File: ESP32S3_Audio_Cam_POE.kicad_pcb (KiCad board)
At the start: 4 copper layers, 56 parts, among them J1 USB-C, U1 USBLC6-2SC6, U2 TLV62568DBVR, U3 ESP32-S3R8, Y1 40MHz, Y2 32.768KHz

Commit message: Draft commit, needs routing, schematic is probably mostly OK. Footprints are roughly located.
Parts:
- removed G***: LOGO, LOGO
- removed LED1: WS2812C-2020-V1, PCM_JLCPCB:LED-SMD_4P-L1.6-W1.5_XL-1615RGBC-WS2812B
- removed TP10: TestPoint, TestPoint:TestPoint_Pad_D1.0mm
- added BOOT2: SW_BOOT, Button_Switch_SMD:SW_SPST_EVQP2, F.Cu at (53.4, 117.4)
- added C1: 4.7uF, PCM_JLCPCB:C_0805, F.Cu at (128.4, 114.4)
- added C2: 1nF, PCM_JLCPCB:C_0402, F.Cu at (126.6, 115.2)
- added C27: 100nF, PCM_JLCPCB:C_0603, F.Cu at (74.1, 93.5)
- added C28: 100nF, PCM_JLCPCB:C_0603, B.Cu at (71.7, 131.5)
- added C29: 100nF, PCM_JLCPCB:C_0603, B.Cu at (71.9, 136.8)
- added C3: 10pF, PCM_JLCPCB:C_0402, F.Cu at (76.9, 78.3)
- added C30: 100nF, PCM_JLCPCB:C_0603, F.Cu at (74.1, 95.8)
- added C31: 100nF, PCM_JLCPCB:C_0603, B.Cu at (69.7, 131.5)
- added C32: 100nF, PCM_JLCPCB:C_0603, B.Cu at (69.7, 132.8)
- added C33: 10pF, PCM_JLCPCB:C_0402, F.Cu at (101.8, 119.0)
- added C34: 10pF, PCM_JLCPCB:C_0402, F.Cu at (105.0, 122.3)
- added C35: 100nF, PCM_JLCPCB:C_0603, B.Cu at (114.2, 125.3)
- added C36: 10uF, PCM_JLCPCB:C_0805, B.Cu at (117.9, 124.3)
- added C37: 100nF, PCM_JLCPCB:C_0603, B.Cu at (112.8, 125.3)
- added C38: 100nF, PCM_JLCPCB:C_0603, F.Cu at (66.9, 94.8)
- added C39: 10nF, PCM_JLCPCB:C_0402, F.Cu at (101.8, 124.3)
- added C4: 10pF, PCM_JLCPCB:C_0402, F.Cu at (70.8, 123.7)
- added C40: 4.7uF, PCM_JLCPCB:C_0603, B.Cu at (115.5, 125.3)
- added C41: 100nF, PCM_JLCPCB:C_0603, F.Cu at (90.2, 142.3)
- added C42: 1uF, PCM_JLCPCB:C_0603, F.Cu at (87.9, 142.3)
- added C43: 1uF, PCM_JLCPCB:C_0603, B.Cu at (90.7, 40.8)
- added C44: 100nF, PCM_JLCPCB:C_0603, B.Cu at (90.7, 43.3)
- added C45: 100pF, PCM_JLCPCB:C_0402, B.Cu at (100.7, 35.8)
- added C46: 100nF, PCM_JLCPCB:C_0603, F.Cu at (99.1, 87.7)
- added C47: 100pF, PCM_JLCPCB:C_0402, B.Cu at (93.4, 39.8)
- added C48: 1uF, PCM_JLCPCB:C_0603, F.Cu at (99.1, 89.2)
- added C49: 100nF, PCM_JLCPCB:C_0603, F.Cu at (91.2, 153.8)
- added C5: 100nF, PCM_JLCPCB:C_0603, F.Cu at (124.6, 115.2)
- added C50: 6.8nF, PCM_JLCPCB:C_0603, F.Cu at (128.8, 122.8)
- added C51: 6.8nF, PCM_JLCPCB:C_0603, F.Cu at (128.8, 125.8)
- added C52: 220nF, PCM_JLCPCB:C_0603, F.Cu at (128.8, 131.8)
- added C53: 220nF, PCM_JLCPCB:C_0603, F.Cu at (128.8, 124.3)
- added C54: 10uF, PCM_JLCPCB:C_0805, F.Cu at (118.9, 98.3)
- added C55: 100nF, PCM_JLCPCB:C_0603, F.Cu at (120.7, 98.3)
- added C56: 100nF, PCM_JLCPCB:C_0603, F.Cu at (62.5, 81.0)
- added C57: 100nF, PCM_JLCPCB:C_0603, F.Cu at (57.9, 124.9)
- added C58: 100nF, PCM_JLCPCB:C_0603, F.Cu at (96.6, 152.0)
- added C59: 100nF, PCM_JLCPCB:C_0805, B.Cu at (143.3, 137.3)
- added C60: 100nF, PCM_JLCPCB:C_0805, F.Cu at (146.3, 137.3)
- added C61: 10uF, PCM_JLCPCB:C_0805, B.Cu at (140.3, 144.8)
- added C62: 100nF, PCM_JLCPCB:C_0805, B.Cu at (146.8, 114.8)
- added C63: 100nF, PCM_JLCPCB:C_0805, B.Cu at (143.3, 115.3)
- added C64: 22uF, PCM_JLCPCB:C_0805, B.Cu at (140.3, 142.8)
- added C65: 1nF, PCM_JLCPCB:C_1206, B.Cu at (139.3, 135.5)
- added C66: 220pF, PCM_JLCPCB:C_0402, B.Cu at (122.9, 99.0)
- added C67: 220pF, PCM_JLCPCB:C_0402, B.Cu at (122.9, 97.0)
- added C68: 100nF, PCM_JLCPCB:C_0603, F.Cu at (62.2, 75.8)
- added C69: 100nF, PCM_JLCPCB:C_0603, F.Cu at (57.9, 117.3)
- added C70: 100nF, PCM_JLCPCB:C_0603, F.Cu at (132.0, 131.8)
- added C71: 100nF, PCM_JLCPCB:C_0603, F.Cu at (133.4, 90.0)
- added C72: 100nF, PCM_JLCPCB:C_0603, F.Cu at (48.4, 83.4)
- added CARD1: TF PUSH, JLCPCB:TF-PUSH-SD-CARD_C393941, F.Cu at (54.9, 97.8)
- added D10: Red, PCM_JLCPCB:D_0603, F.Cu at (134.9, 114.2)
- added D11: 1N4148W, PCM_JLCPCB:D_SOD-123, B.Cu at (143.6, 144.3)
- added D12: White, PCM_JLCPCB:D_0603, F.Cu at (81.3, 151.8)
- added D13: IR, JLCPCB:IR-LED_C131280, F.Cu at (84.5, 158.5)
- added D3: Yellow, PCM_JLCPCB:D_0805, F.Cu at (102.1, 114.8)
- added D4: Green, PCM_JLCPCB:D_0805, F.Cu at (102.1, 117.5)
- added D5: MB6S, JLCPCB:MB6S-C82584, B.Cu at (131.6, 151.3)
- added D6: MB6S, JLCPCB:MB6S-C82584, B.Cu at (142.1, 151.3)
- added D7: SMAJ58A, PCM_JLCPCB:D_SMA, B.Cu at (138.3, 156.0)
- added D8: Green, PCM_JLCPCB:D_0805, F.Cu at (124.9, 111.2)
- added D9: WS2812B, PCM_JLCPCB:LED-SMD_4P-L1.6-W1.5_XL-1615RGBC-WS2812B, F.Cu at (98.9, 151.0)
- added DISP1: SLS0563DRA1GD, JLCPCB:3x7-seg_LED-RED_C2913084, F.Cu at (100.7, 43.3)
- added FPC1: AFC01-S24FCC-00, JLCPCB:OV2640_connector_AFC01-S24FCC-00, F.Cu at (69.9, 64.8)
- added J10: Conn_01x02, Connector_PinHeader_1.00mm:PinHeader_1x02_P1.00mm_Vertical, B.Cu at (126.4, 98.6)
- added J11: Conn_01x02, Connector_PinHeader_1.00mm:PinHeader_1x02_P1.00mm_Vertical, F.Cu at (84.0, 162.8)
- added J12: Conn_01x02, Connector_PinHeader_1.00mm:PinHeader_1x02_P1.00mm_Vertical, F.Cu at (84.0, 156.3)
- added J13: Conn_01x02, Connector_PinHeader_1.00mm:PinHeader_1x02_P1.00mm_Vertical, F.Cu at (84.0, 153.0)
- added J2: USB-C, Connector_USB:USB_C_Receptacle_GCT_USB4105-xx-A_16P_TopMnt_Horizontal, F.Cu at (112.8, 155.5)
- added J3: Conn_01x02, Connector_PinHeader_1.00mm:PinHeader_1x02_P1.00mm_Vertical, F.Cu at (82.1, 96.4)
- added J4: Conn_01x02, Connector_PinHeader_1.00mm:PinHeader_1x02_P1.00mm_Vertical, F.Cu at (73.4, 121.0)
- added J5: Conn_01x03, Connector_PinHeader_2.54mm:PinHeader_1x03_P2.54mm_Vertical, F.Cu at (55.5, 154.5)
- added J6: Conn_01x03, Connector_PinHeader_2.54mm:PinHeader_1x03_P2.54mm_Vertical, F.Cu at (60.1, 154.5)
- added J7: Conn_01x03, Connector_PinHeader_2.54mm:PinHeader_1x03_P2.54mm_Vertical, F.Cu at (64.7, 154.5)
- added J8: Conn_01x03, Connector_PinHeader_2.54mm:PinHeader_1x03_P2.54mm_Vertical, F.Cu at (69.3, 154.5)
- added J9: HC-RJ45-055-4_8P8C_Shielded, JLCPCB:HC-RJ45-055-4_C3000211, F.Cu at (143.5, 126.3)
- added JP1: Jumper_2_Small_Bridged, Jumper:SolderJumper-2_P1.3mm_Bridged_RoundedPad1.0x1.5mm, F.Cu at (78.2, 96.7)
- added JP2: Jumper_2_Small_Bridged, Jumper:SolderJumper-2_P1.3mm_Bridged_RoundedPad1.0x1.5mm, F.Cu at (78.2, 100.2)
- added JP3: SolderJumper_2_Open, Jumper:SolderJumper-2_P1.3mm_Open_TrianglePad1.0x1.5mm, B.Cu at (117.9, 105.5)
- added JP4: SolderJumper_2_Open, Jumper:SolderJumper-2_P1.3mm_Open_TrianglePad1.0x1.5mm, B.Cu at (117.9, 103.0)
- added JP5: SolderJumper_2_Open, Jumper:SolderJumper-2_P1.3mm_Open_TrianglePad1.0x1.5mm, F.Cu at (117.9, 103.0)
- added JP6: SolderJumper_2_Open, Jumper:SolderJumper-2_P1.3mm_Open_TrianglePad1.0x1.5mm, F.Cu at (117.9, 105.5)
- added JP7: SolderJumper_3_Bridged12, Jumper:SolderJumper-3_P1.3mm_Bridged12_Pad1.0x1.5mm, F.Cu at (139.4, 90.3)
- added JP8: SolderJumper_3_Bridged12, Jumper:SolderJumper-3_P1.3mm_Bridged12_Pad1.0x1.5mm, F.Cu at (48.6, 77.9)
- added L4: 3.9nH,300mA, PCM_JLCPCB:L_0402, B.Cu at (114.4, 123.3)
- added PB1: SW_RST, Button_Switch_SMD:SW_SPST_EVQP2, F.Cu at (75.6, 36.6)
- added PB2: SW_RST, Button_Switch_SMD:SW_SPST_EVQP2, F.Cu at (127.4, 36.8)
- added Q1: AO3401A, PCM_JLCPCB:Q_SOT-23, B.Cu at (80.7, 69.1)
- added Q2: AO3401A, PCM_JLCPCB:Q_SOT-23, F.Cu at (51.1, 157.1)
- added Q3: AO3401A, PCM_JLCPCB:Q_SOT-23, F.Cu at (77.3, 153.8)
- added Q4: AO3401A, PCM_JLCPCB:Q_SOT-23, F.Cu at (77.3, 158.5)
- added Q5: AO3401A, PCM_JLCPCB:Q_SOT-23, F.Cu at (77.3, 163.8)
- added R13: 33Ω, PCM_JLCPCB:R_0402, F.Cu at (114.3, 149.0)
- added R14: 10MΩ, PCM_JLCPCB:R_0402, B.Cu at (81.9, 66.6)
- added R15: 1MΩ, PCM_JLCPCB:R_0402, B.Cu at (79.9, 66.6)
- added R16: 10kΩ, PCM_JLCPCB:R_0402, B.Cu at (70.2, 60.1)
- added R17: 10kΩ, PCM_JLCPCB:R_0402, B.Cu at (70.2, 61.1)
- added R18: 10kΩ, PCM_JLCPCB:R_0402, B.Cu at (70.2, 62.1)
- added R19: 10kΩ, PCM_JLCPCB:R_0402, B.Cu at (68.5, 62.1)
- added R20: 1MΩ, PCM_JLCPCB:R_0402, F.Cu at (99.3, 121.5)
- added R21: 0Ω, PCM_JLCPCB:R_0402, F.Cu at (105.0, 123.3)
- added R22: 20Ω, PCM_JLCPCB:R_0603, F.Cu at (105.4, 126.8)
- added R23: 20Ω, PCM_JLCPCB:R_0603, F.Cu at (105.4, 128.3)
- added R24: 20Ω, PCM_JLCPCB:R_0603, F.Cu at (105.4, 129.8)
- added R25: 20Ω, PCM_JLCPCB:R_0603, F.Cu at (105.4, 131.3)
- added R26: 20Ω, PCM_JLCPCB:R_0603, F.Cu at (105.4, 132.8)
- added R27: 20Ω, PCM_JLCPCB:R_0603, F.Cu at (105.4, 134.3)
- added R28: 10kΩ, PCM_JLCPCB:R_0402, F.Cu at (114.8, 117.8)
- added R29: 10kΩ, PCM_JLCPCB:R_0402, F.Cu at (63.1, 97.8)
- added R3: 22Ω, PCM_JLCPCB:R_0402, B.Cu at (130.1, 111.4)
- added R30: 10kΩ, PCM_JLCPCB:R_0402, F.Cu at (64.6, 97.3)
- added R31: 10kΩ, PCM_JLCPCB:R_0402, F.Cu at (64.6, 95.3)
- added R32: 10kΩ, PCM_JLCPCB:R_0402, F.Cu at (65.6, 94.8)
- added R33: 100kΩ, PCM_JLCPCB:R_0402, F.Cu at (86.2, 135.2)
- added R34: 680Ω, PCM_JLCPCB:R_0402, F.Cu at (105.1, 114.8)
- added R35: 680Ω, PCM_JLCPCB:R_0402, F.Cu at (105.1, 120.0)
- added R36: 12kΩ, PCM_JLCPCB:R_0603, F.Cu at (122.5, 124.8)
- added R37: 100kΩ, PCM_JLCPCB:R_0402, F.Cu at (99.1, 90.4)
- added R38: 10kΩ, PCM_JLCPCB:R_0402, B.Cu at (92.4, 42.0)
- added R39: 10kΩ, PCM_JLCPCB:R_0402, B.Cu at (93.4, 42.0)
- added R4: 5.1kΩ, PCM_JLCPCB:R_0402, B.Cu at (144.7, 98.5)
- added R40: 100kΩ, PCM_JLCPCB:R_0805, B.Cu at (115.2, 104.3)
- added R41: 100kΩ, PCM_JLCPCB:R_0805, F.Cu at (115.2, 104.3)
- added R42: 10MΩ, PCM_JLCPCB:R_0402, F.Cu at (48.3, 157.1)
- added R43: 1MΩ, PCM_JLCPCB:R_0402, B.Cu at (116.9, 98.0)
- added R44: 47Ω, PCM_JLCPCB:R_0603, F.Cu at (128.8, 128.8)
- added R45: 47Ω, PCM_JLCPCB:R_0603, F.Cu at (128.8, 130.3)
- added R46: 47Ω, PCM_JLCPCB:R_0603, F.Cu at (128.8, 133.3)
- added R47: 1MΩ, PCM_JLCPCB:R_0402, F.Cu at (48.3, 155.1)
- added R48: 82Ω, PCM_JLCPCB:R_0603, F.Cu at (131.3, 122.8)
- added R49: 82Ω, PCM_JLCPCB:R_0603, F.Cu at (131.3, 125.8)
- added R50: 10kΩ, PCM_JLCPCB:R_0402, F.Cu at (124.9, 112.7)
- added R51: 10kΩ, PCM_JLCPCB:R_0402, F.Cu at (62.5, 83.5)
- added R52: 10kΩ, PCM_JLCPCB:R_0402, F.Cu at (57.9, 127.4)
- added R53: 10kΩ, PCM_JLCPCB:R_0402, F.Cu at (136.1, 114.2)
- added R54: 10MΩ, PCM_JLCPCB:R_0402, F.Cu at (74.5, 153.8)
- added R55: 10MΩ, PCM_JLCPCB:R_0402, F.Cu at (74.5, 158.8)
- added R56: 10MΩ, PCM_JLCPCB:R_0402, F.Cu at (74.5, 163.8)
- added R57: 1MΩ, PCM_JLCPCB:R_0402, F.Cu at (74.5, 151.8)
- added R58: 1MΩ, PCM_JLCPCB:R_0402, F.Cu at (74.5, 156.8)
- added R59: 75Ω, PCM_JLCPCB:R_0603, F.Cu at (134.3, 129.3)
- added R60: 75Ω, PCM_JLCPCB:R_0603, F.Cu at (135.5, 129.3)
- added R61: 75Ω, PCM_JLCPCB:R_0603, F.Cu at (135.3, 133.3)
- added R62: 75Ω, PCM_JLCPCB:R_0603, F.Cu at (135.3, 131.8)
- added R63: 1MΩ, PCM_JLCPCB:R_0402, F.Cu at (74.5, 161.8)
- added R64: 10kΩ, PCM_JLCPCB:R_0402, F.Cu at (80.5, 158.5)
- added R65: 10kΩ, PCM_JLCPCB:R_0402, F.Cu at (80.5, 153.8)
- added RST2: SW_RST, Button_Switch_SMD:SW_SPST_EVQP2, F.Cu at (53.4, 124.9)
- added T1: H1102NLT, JLCPCB:H1102NLT_C18584, B.Cu at (130.6, 127.3)
- added TP11: TestPoint, TestPoint:TestPoint_Pad_D1.0mm, B.Cu at (68.5, 57.8)
- added TP12: TestPoint, TestPoint:TestPoint_Pad_D1.0mm, B.Cu at (71.2, 68.6)
- added TP13: TestPoint, TestPoint:TestPoint_Pad_D1.0mm, B.Cu at (70.5, 70.6)
- added TP14: TestPoint, TestPoint:TestPoint_Plated_Hole_D2.0mm, B.Cu at (71.2, 55.1)
- added TP15: TestPoint, TestPoint:TestPoint_Plated_Hole_D2.0mm, B.Cu at (71.2, 74.6)
- added TP16: TestPoint, TestPoint:TestPoint_Pad_D1.0mm, F.Cu at (73.7, 98.4)
- added TP17: TestPoint, TestPoint:TestPoint_Pad_D1.0mm, F.Cu at (80.4, 145.0)
- added TP18: TestPoint, TestPoint:TestPoint_Pad_D1.0mm, F.Cu at (91.4, 132.8)
- added TP19: TestPoint, TestPoint:TestPoint_Pad_D1.0mm, F.Cu at (91.4, 129.5)
- added TP20: TestPoint, TestPoint:TestPoint_Pad_D1.0mm, F.Cu at (91.4, 126.5)
- added TP21: TestPoint, TestPoint:TestPoint_Pad_D1.0mm, F.Cu at (91.4, 123.3)
- added TP22: TestPoint, TestPoint:TestPoint_Pad_D1.0mm, F.Cu at (91.4, 120.3)
- added TP23: TestPoint, TestPoint:TestPoint_Pad_D1.0mm, F.Cu at (91.4, 117.5)
- added TP24: TestPoint, TestPoint:TestPoint_Pad_D1.0mm, F.Cu at (91.4, 114.8)
- added TP25: TestPoint, TestPoint:TestPoint_Pad_D1.0mm, F.Cu at (91.4, 111.8)
- added TP26: TestPoint, TestPoint:TestPoint_Pad_D1.0mm, F.Cu at (84.7, 111.0)
- added TP27: TestPoint, TestPoint:TestPoint_Pad_D1.0mm, F.Cu at (81.4, 111.0)
- added TP28: TestPoint, TestPoint:TestPoint_Pad_D1.0mm, F.Cu at (76.9, 111.0)
- added TP29: TestPoint, TestPoint:TestPoint_Pad_D1.0mm, F.Cu at (73.9, 111.0)
- added TP30: TestPoint, TestPoint:TestPoint_Pad_D1.0mm, F.Cu at (71.2, 111.0)
- added TP31: TestPoint, TestPoint:TestPoint_Pad_D1.0mm, F.Cu at (68.2, 111.0)
- added TP32: TestPoint, TestPoint:TestPoint_Pad_D1.0mm, F.Cu at (57.2, 111.0)
- added TP33: TestPoint, TestPoint:TestPoint_Pad_D1.0mm, F.Cu at (119.9, 138.8)
- added TP34: TestPoint, TestPoint:TestPoint_Pad_D1.0mm, F.Cu at (117.9, 138.8)
- added TP35: TestPoint, TestPoint:TestPoint_Pad_D1.0mm, F.Cu at (115.9, 138.8)
- added TP36: TestPoint, TestPoint:TestPoint_Pad_D1.0mm, F.Cu at (105.9, 138.8)
- added TP37: TestPoint, TestPoint:TestPoint_Pad_D1.0mm, F.Cu at (107.9, 138.8)
- added TP38: TestPoint, TestPoint:TestPoint_Pad_D1.0mm, F.Cu at (109.9, 138.8)
- added TP39: TestPoint, TestPoint:TestPoint_Pad_D1.0mm, F.Cu at (111.9, 138.8)
- added TP40: TestPoint, TestPoint:TestPoint_Pad_D1.0mm, F.Cu at (113.9, 138.8)
- added TP41: TestPoint, TestPoint:TestPoint_Pad_D1.0mm, F.Cu at (111.4, 113.8)
- added TP42: TestPoint, TestPoint:TestPoint_Pad_D1.0mm, F.Cu at (105.8, 117.8)
- added TP43: TestPoint, TestPoint:TestPoint_Pad_D1.0mm, F.Cu at (117.7, 113.8)
- added TP44: TestPoint, TestPoint:TestPoint_Pad_D1.0mm, F.Cu at (95.9, 141.9)
- added TP45: TestPoint, TestPoint:TestPoint_Pad_D1.0mm, F.Cu at (62.9, 100.5)
- added TP46: TestPoint, TestPoint:TestPoint_Pad_D1.0mm, F.Cu at (63.4, 92.0)
- added TP47: TestPoint, TestPoint:TestPoint_Pad_D1.0mm, F.Cu at (63.4, 90.0)
- added TP48: TestPoint, TestPoint:TestPoint_Pad_D1.0mm, B.Cu at (107.9, 49.3)
- added TP49: TestPoint, TestPoint:TestPoint_Pad_D1.0mm, F.Cu at (92.8, 141.9)
- added TP50: TestPoint, TestPoint:TestPoint_Pad_D1.0mm, F.Cu at (91.2, 33.5)
- added TP51: TestPoint, TestPoint:TestPoint_Plated_Hole_D2.0mm, F.Cu at (49.6, 88.3)
- added TP52: TestPoint, TestPoint:TestPoint_Plated_Hole_D2.0mm, F.Cu at (59.1, 88.3)
- added TP53: TestPoint, TestPoint:TestPoint_Plated_Hole_D2.0mm, F.Cu at (49.6, 107.3)
- added TP54: TestPoint, TestPoint:TestPoint_Plated_Hole_D2.0mm, F.Cu at (59.4, 106.8)
- added TP55: TestPoint, TestPoint:TestPoint_Pad_D1.0mm, B.Cu at (137.0, 126.5)
- added TP56: TestPoint, TestPoint:TestPoint_Pad_D1.0mm, B.Cu at (137.0, 128.5)
- added TP57: TestPoint, TestPoint:TestPoint_Pad_D1.0mm, B.Cu at (93.2, 46.5)
- added TP58: TestPoint, TestPoint:TestPoint_Pad_D1.0mm, B.Cu at (92.9, 49.8)
- added TP59: TestPoint, TestPoint:TestPoint_Pad_D1.0mm, F.Cu at (102.6, 97.7)
- added TP6: TestPoint, TestPoint:TestPoint_Pad_D1.0mm, F.Cu at (45.7, 133.1)
- added TP60: TestPoint, TestPoint:TestPoint_Pad_D1.0mm, F.Cu at (95.6, 97.7)
- added TP61: TestPoint, TestPoint:TestPoint_Pad_D1.0mm, B.Cu at (124.0, 126.3)
- added TP62: TestPoint, TestPoint:TestPoint_Pad_D1.0mm, B.Cu at (124.0, 128.3)
- added TP63: TestPoint, TestPoint:TestPoint_Pad_D1.0mm, F.Cu at (97.6, 149.0)
- added TP64: TestPoint, TestPoint:TestPoint_Pad_D1.0mm, B.Cu at (117.7, 96.5)
- added TP65: TestPoint, TestPoint:TestPoint_Pad_D1.0mm, B.Cu at (119.7, 95.8)
- added TP66: TestPoint, TestPoint:TestPoint_Pad_D1.0mm, F.Cu at (126.1, 142.3)
- added TP67: TestPoint, TestPoint:TestPoint_Pad_D1.0mm, B.Cu at (121.2, 101.8)
- added TP68: TestPoint, TestPoint:TestPoint_Pad_D1.0mm, B.Cu at (123.2, 101.3)
- added TST-R1: 0Ω, PCM_JLCPCB:R_0603, B.Cu at (128.1, 109.7)
- added TST-R10: 0Ω, PCM_JLCPCB:R_0603, F.Cu at (82.2, 100.1)
- added TST-R11: 0Ω, PCM_JLCPCB:R_0603, B.Cu at (66.9, 131.5)
- added TST-R12: 0Ω, PCM_JLCPCB:R_0603, B.Cu at (115.0, 121.3)
- added TST-R13: 0Ω, PCM_JLCPCB:R_0603, F.Cu at (69.1, 95.5)
- added TST-R14: 0Ω, PCM_JLCPCB:R_0603, B.Cu at (90.4, 45.8)
- added TST-R15: 0Ω, PCM_JLCPCB:R_0603, F.Cu at (92.2, 156.0)
- added TST-R16: 0Ω, PCM_JLCPCB:R_0603, F.Cu at (116.7, 98.8)
- added TST-R17: 0Ω, PCM_JLCPCB:R_0603, F.Cu at (48.0, 159.6)
- added TST-R18: 0Ω, PCM_JLCPCB:R_0603, F.Cu at (117.9, 100.8)
- added TST-R19: 0Ω, PCM_JLCPCB:R_0603, F.Cu at (98.9, 152.8)
- added TST-R2: 0Ω, PCM_JLCPCB:R_0603, B.Cu at (135.6, 116.2)
- added TST-R20: 0Ω, PCM_JLCPCB:R_0603, F.Cu at (136.4, 92.5)
- added TST-R21: 0Ω, PCM_JLCPCB:R_0603, F.Cu at (81.0, 155.5)
- added TST-R22: 0Ω, PCM_JLCPCB:R_0603, F.Cu at (81.0, 160.3)
- added TST-R23: 0Ω, PCM_JLCPCB:R_0603, F.Cu at (81.0, 165.3)
- added TST-R24: 0Ω, PCM_JLCPCB:R_0603, B.Cu at (140.3, 147.3)
- added TST-R25: 0Ω, PCM_JLCPCB:R_0603, F.Cu at (133.7, 92.5)
- added TST-R26: 0Ω, PCM_JLCPCB:R_0603, F.Cu at (50.7, 83.4)
- added TST-R27: 0Ω, PCM_JLCPCB:R_0603, F.Cu at (50.7, 80.7)
- added TST-R3: 0Ω, PCM_JLCPCB:R_0603, F.Cu at (135.2, 104.5)
- added TST-R4: 0Ω, PCM_JLCPCB:R_0603, F.Cu at (116.8, 145.5)
- added TST-R5: 0Ω, PCM_JLCPCB:R_0603, F.Cu at (83.9, 83.3)
- added TST-R6: 0Ω, PCM_JLCPCB:R_0603, B.Cu at (83.4, 69.1)
- added TST-R7: 0Ω, PCM_JLCPCB:R_0603, B.Cu at (71.7, 61.1)
- added TST-R8: 0Ω, PCM_JLCPCB:R_0603, B.Cu at (76.1, 62.9)
- added TST-R9: 0Ω, PCM_JLCPCB:R_0603, B.Cu at (76.1, 68.1)
- added U10: W25Q128, PCM_JLCPCB:SOIC-8_L5.3-W5.3-P1.27-LS8.0-BL, F.Cu at (92.7, 137.5)
- added U11: TM1637, JLCPCB:digital tube drivers_c2962580, B.Cu at (100.7, 43.3)
- added U12: DS18B20U(UMW), JLCPCB:DS18B20_C695836, F.Cu at (91.2, 151.3)
- added U13: W25Q128, PCM_JLCPCB:SOIC-8_L5.3-W5.3-P1.27-LS8.0-BL, F.Cu at (99.1, 93.9)
- added U14: DP9900M-5V, JLCPCB:DP9900M_C5380106, F.Cu at (138.8, 149.3)
- added U15: MAX98357AETE+T, JLCPCB:MAX98357AETE+T_C910544, B.Cu at (120.2, 98.9)
- added U16: ICS-43434, JLCPCB:ICS-43434_C5656610, F.Cu at (135.7, 89.8)
- added U17: ICS-43434, JLCPCB:ICS-43434_C5656610, F.Cu at (48.2, 81.2)
- added U4: USBLC6-2SC6, Package_TO_SOT_SMD:SOT-23-6, F.Cu at (112.6, 145.0)
- added U5: XC6206-1.5NR, Package_TO_SOT_SMD:SOT-23-3, B.Cu at (76.8, 65.4)
- added U6: XC6206-2.8V, Package_TO_SOT_SMD:SOT-23-3, B.Cu at (76.7, 70.7)
- added U7: ESP32-S3, PCM_JLCPCB:QFN-56-1EP_7x7mm_P0.4mm_EP4x4mm_ThermalVias, F.Cu at (80.7, 90.3)
- added U8: ESP32-S3, PCM_JLCPCB:QFN-56-1EP_7x7mm_P0.4mm_EP4x4mm_ThermalVias, F.Cu at (72.6, 134.2)
- added U9: W5500, Package_QFP:LQFP-48_7x7mm_P0.5mm, F.Cu at (115.9, 126.3)
- added X1: X322525MOB4SI, PCM_JLCPCB:OSC-SMD_4P-L3.2-W2.5-BL, F.Cu at (101.8, 121.6)
- added Y3: 32.768KHz, Crystal:Crystal_SMD_3215-2Pin_3.2x1.5mm, F.Cu at (72.2, 144.5)
- C10: value 10u -> 20pF; footprint Capacitor_SMD:C_0402_1005Metric_Pad0.74x0.62mm_HandSolder -> PCM_JLCPCB:C_0402; moved to F.Cu
- C11, C20: value 1u -> 100nF; footprint Capacitor_SMD:C_0402_1005Metric_Pad0.74x0.62mm_HandSolder -> PCM_JLCPCB:C_0603
- C12, C15: value 3p3 -> 3.3pF; footprint Capacitor_SMD:C_0603_1608Metric_Pad1.08x0.95mm_HandSolder -> PCM_JLCPCB:C_0402
- C13: value 100n -> 100nF; footprint Capacitor_SMD:C_0402_1005Metric_Pad0.74x0.62mm_HandSolder -> PCM_JLCPCB:C_0603; moved to F.Cu
- C14: value 100n -> 10uF; footprint Capacitor_SMD:C_0402_1005Metric_Pad0.74x0.62mm_HandSolder -> PCM_JLCPCB:C_0402; moved to F.Cu
- C16, C18, C26: value 100n -> 1uF; footprint Capacitor_SMD:C_0402_1005Metric_Pad0.74x0.62mm_HandSolder -> PCM_JLCPCB:C_0603; moved to B.Cu
- C17, C23: value 100n -> 1uF; footprint Capacitor_SMD:C_0402_1005Metric_Pad0.74x0.62mm_HandSolder -> PCM_JLCPCB:C_0603
- C19, C21: value 10p -> 100nF; footprint Capacitor_SMD:C_0402_1005Metric_Pad0.74x0.62mm_HandSolder -> PCM_JLCPCB:C_0603
- C22: value 20p -> 15pF; footprint Capacitor_SMD:C_0402_1005Metric_Pad0.74x0.62mm_HandSolder -> PCM_JLCPCB:C_0402
- C24: value 20p -> 100nF; footprint Capacitor_SMD:C_0402_1005Metric_Pad0.74x0.62mm_HandSolder -> PCM_JLCPCB:C_0603; moved to F.Cu
- C25: value 100n -> 100nF; footprint Capacitor_SMD:C_0402_1005Metric_Pad0.74x0.62mm_HandSolder -> PCM_JLCPCB:C_0603
- C6: value 4u7 -> 10pF; footprint Capacitor_SMD:C_0402_1005Metric_Pad0.74x0.62mm_HandSolder -> PCM_JLCPCB:C_0402; moved to F.Cu
- C7: value 10u -> 10pF; footprint Capacitor_SMD:C_0402_1005Metric_Pad0.74x0.62mm_HandSolder -> PCM_JLCPCB:C_0402; moved to F.Cu
- C8: value 100n -> 10uF; footprint Capacitor_SMD:C_0402_1005Metric_Pad0.74x0.62mm_HandSolder -> PCM_JLCPCB:C_0402
- C9: value 100n -> 20pF; footprint Capacitor_SMD:C_0402_1005Metric_Pad0.74x0.62mm_HandSolder -> PCM_JLCPCB:C_0402; moved to F.Cu
- D1, D2: value LED -> 1N4148W; footprint LED_SMD:LED_0402_1005Metric_Pad0.77x0.64mm_HandSolder -> PCM_JLCPCB:D_SOD-123; moved to F.Cu
- J1, L1, L2, TP2, TP3, TP4, TP8, Y1: moved to F.Cu
- R1, R2: value 5k1 -> 22Ω; footprint Resistor_SMD:R_0402_1005Metric_Pad0.72x0.64mm_HandSolder -> PCM_JLCPCB:R_0402; moved to F.Cu
- R10: value 10k -> 33Ω; footprint Resistor_SMD:R_0402_1005Metric_Pad0.72x0.64mm_HandSolder -> PCM_JLCPCB:R_0402
- R11, R12: value 10k -> 33Ω; footprint Resistor_SMD:R_0402_1005Metric_Pad0.72x0.64mm_HandSolder -> PCM_JLCPCB:R_0402; moved to F.Cu
- R5: value 22R -> 5.1kΩ; footprint Resistor_SMD:R_0402_1005Metric_Pad0.72x0.64mm_HandSolder -> PCM_JLCPCB:R_0402
- R6: value 450k -> 5.1kΩ; footprint Resistor_SMD:R_0402_1005Metric_Pad0.72x0.64mm_HandSolder -> PCM_JLCPCB:R_0402
- R7: value 100k -> 5.1kΩ; footprint Resistor_SMD:R_0402_1005Metric_Pad0.72x0.64mm_HandSolder -> PCM_JLCPCB:R_0402; moved to F.Cu
- R8: value 100k -> 450k
- R9: value 22R -> 100kΩ; footprint Resistor_SMD:R_0402_1005Metric_Pad0.72x0.64mm_HandSolder -> PCM_JLCPCB:R_0402
- U1: value USBLC6-2SC6 -> TLV62568DBVR; footprint Package_TO_SOT_SMD:SOT-23-6 -> Package_TO_SOT_SMD:SOT-23-5
- U2: value TLV62568DBVR -> MT9221CT-06BR5; footprint Package_TO_SOT_SMD:SOT-23-5 -> JLCPCB:Current-sensor_MT9221CT-06BR5_C879632
- U3: value ESP32-S3R8 -> USBLC6-2SC6; footprint PCM_JLCPCB:QFN-56-1EP_7x7mm_P0.4mm_EP4x4mm_ThermalVias -> Package_TO_SOT_SMD:SOT-23-6
- Y2: value 32.768KHz -> 40MHz; footprint Crystal:Crystal_SMD_3215-2Pin_3.2x1.5mm -> Crystal:Crystal_SMD_3225-4Pin_3.2x2.5mm; moved to F.Cu
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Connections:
- C10 pad 1: +3V3 -> /2OSC32_OUT
- C11 pad 1: +3V3 -> Earth
- C11 pad 2: Earth -> +3V3_RF
- C13 pad 1: +3V3 -> Earth
- C13 pad 2: Earth -> +3V3
- C16 pad 1: +3V3 -> Net-(Q1-D)
- C17 pad 1: VDD_SPI -> Net-(U5-VO)
- C18 pad 1: +3V3 -> Net-(U6-VO)
- C19 pad 1: Net-(C19-Pad1) -> Earth
- C19 pad 2: Earth -> Net-(U5-VO)
- C20 pad 1: VDD_SPI -> Earth
- C20 pad 2: Earth -> Net-(U6-VO)
- C21 pad 1: /OSC_OUT -> Earth
- C21 pad 2: Earth -> /CAM.RST
- C22 pad 1: /OSC32_IN -> Earth
- C22 pad 2: Earth -> /CAM.PCLK
- C23 pad 1: +3V3 -> Earth
- C23 pad 2: Earth -> Net-(U7-VDD3P3_RTC)
- C24 pad 1: /OSC32_OUT -> Net-(U7-VDD3P3_RTC)
- C25 pad 1: /CHIP_PU -> Net-(U7-VDD3P3_RTC)
- C26 pad 1: /CHIP_BOOT -> Earth
- C26 pad 2: Earth -> Net-(U8-VDD3P3_RTC)
- C6 pad 1: VBUS -> /OSC_OUT
- C7 pad 1: +3V3 -> /2OSC_OUT
- C8 pad 1: +3V3_RF -> Net-(C8-Pad1)
- C9 pad 1: +3V3 -> /2OSC32_IN
- D1 pad 1: Earth -> VBUS
- D1 pad 2: Net-(D1-A) -> Net-(D1-Pad2)
- D2 pad 1: Earth -> VBUS
- D2 pad 2: Net-(D2-A) -> Net-(D2-Pad2)
- J1 pad A4: VBUS -> Net-(D1-Pad2)
- J1 pad A9: VBUS -> Net-(D1-Pad2)
- J1 pad B4: VBUS -> Net-(D1-Pad2)
- J1 pad B9: VBUS -> Net-(D1-Pad2)
- L1 pad 1: Net-(U2-SW) -> Net-(U1-SW)
- L1 pad 2: +3V3 -> Net-(C8-Pad1)
- L2 pad 1: +3V3_RF -> Net-(L2-Pad1)
- R1 pad 1: /USB_CC2 -> Net-(C3-Pad1)
- R1 pad 2: Earth -> /OSC_IN
- R10 pad 1: +3V3 -> /USB_PRT_D-
- R10 pad 2: /CHIP_PU -> /USB_D-
- R11 pad 1: VBUS -> /USB_PRT_D+
- R11 pad 2: Net-(D1-A) -> /USB_D+
- R12 pad 1: +3V3 -> /2USB_PRT_D-
- R12 pad 2: Net-(D2-A) -> /2USB_D-
- R2 pad 1: /USB_CC1 -> Net-(C4-Pad1)
- R2 pad 2: Earth -> /2OSC_IN
- R5 pad 1: VBUS -> /2USB_CC2
- R5 pad 2: Net-(U2-EN) -> Earth
- R6 pad 1: +3V3 -> /USB_CC1
- R6 pad 2: Net-(U2-FB) -> Earth
- R7 pad 1: Net-(U2-FB) -> /2USB_CC1
- R8 pad 1: /FLASH_QSPI_nCS -> Net-(C8-Pad1)
- R8 pad 2: VDD_SPI -> Net-(U1-FB)
- R9 pad 1: /OSC_IN -> Net-(U1-FB)
- R9 pad 2: Net-(C19-Pad1) -> Earth
- TP1 pad 1: /USB_D- -> Net-(U1-VIN)
- TP2 pad 1: /USB_D+ -> +3V3
- TP3 pad 1: VBUS -> Net-(L2-Pad1)
- TP4 pad 1: +3V3 -> /2GPIO1
- TP5 pad 1: +3V3_RF -> /2GPIO2
- TP7 pad 1: +3V3 -> /2GPIO7
- TP8 pad 1: /FLASH_QSPI_nCS -> /2GPIO8
- TP9 pad 1: VDD_SPI -> /2GPIO14
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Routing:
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- removed copper zone on B.Cu, net +3V3
- removed copper zone on F.Cu, net +3V3
- removed copper zone on In2.Cu, net +3V3
- removed copper zone on In1.Cu, net Earth
- removed copper zone on B.Cu, net Net-(U2-SW)
- removed copper zone on B.Cu, net VBUS
- removed copper zone on In2.Cu, net VBUS
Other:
- board outline added: 109.2 x 129.5 mm
- board text removed: "ANT"
- board text removed: "BOOT"
- board text removed: "CPU"
- board text removed: "ESP32 S3"
- board text removed: "ESP32S3.M.2 D.Heetkamp 27-2-25 V2"
- board text removed: "FLASH"
- board text removed: "I/O 45/46 STRAPPING"
- board text removed: "I2C(P/U Res)"
- board text removed: "INT 3V3 ENABLE"
- board text removed: "M.2 3V3 ENABLE"
- board text removed: "M.2 USB ENABLE"
- board text removed: "M.2 VBUS ENABLE"
- board text removed: "RGB IO46"
- board text removed: "RST"
- board text removed: "SPICLK(P/D Res)"
- board text removed: "USB"
- board text removed: "VBUS 3V3"
- board text removed: "Y1: 40MHz Y2: 32.8KHz"

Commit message: draft commit
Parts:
- removed RST1: SW_RST, Button_Switch_SMD:SW_SPST_EVQP2
- added RST3: Tactile Button, 160gf, PCM_JLCPCB:SW-SMD_4P-L5.1-W5.1-P3.70-LS6.5-TL-2, F.Cu at (51.4, 120.7)
- BOOT1, BOOT2: value SW_BOOT -> Tactile Button, 160gf; footprint Button_Switch_SMD:SW_SPST_EVQP2 -> PCM_JLCPCB:SW-SMD_4P-L5.1-W5.1-P3.70-LS6.5-TL-2
- J1, J2: value USB-C -> Connector, USB-TYPE-C-16P; footprint Connector_USB:USB_C_Receptacle_GCT_USB4105-xx-A_16P_TopMnt_Horizontal -> PCM_JLCPCB:TYPE-C-SMD_HX-TYPE-C-16PIN
- L1: value 2u2 -> 2.2uH
- L2, L3: value 2n2 -> 2nH
- PB1, PB2, RST2: value SW_RST -> Tactile Button, 160gf; footprint Button_Switch_SMD:SW_SPST_EVQP2 -> PCM_JLCPCB:SW-SMD_4P-L5.1-W5.1-P3.70-LS6.5-TL-2
- U10, U13: value W25Q128 -> W25Q128JVSIQ
- moved PB2 54.5 mm to (73.0, 39.4), turned to 0 degrees
- moved PB1 53.4 mm to (128.9, 39.4), turned to 0 degrees
- moved RST2 48.9 mm to (57.1, 76.2)
- moved BOOT1 6.60 mm to (57.1, 69.2)
- moved J4 6.57 mm to (73.9, 114.5)
- moved C26 6.57 mm to (70.1, 127.5)
- moved C28 6.57 mm to (72.1, 125.0)
- moved C31 6.57 mm to (70.1, 125.0)
- moved C32 6.57 mm to (70.1, 126.2)
- moved C4 6.57 mm to (71.3, 117.1)
- moved C7 6.57 mm to (66.8, 117.1)
- moved R2 6.57 mm to (70.3, 120.4)
- moved TST-R11 6.57 mm to (67.4, 125.0)
- moved U8 6.57 mm to (73.0, 127.6)
- moved Y2 6.57 mm to (69.0, 117.1)
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- renumbered C70 to C68, C71 to C69, C72 to C70, C68 to C71, C69 to C72, R6 to R5, R5 to R6, TP11 to TP10, TP12 to TP11, TP13 to TP12, TP14 to TP13, TP15 to TP14, TP16 to TP15, TP17 to TP16, TP18 to TP17, TP19 to TP18, TP20 to TP19, TP21 to TP20, TP22 to TP21, TP23 to TP22, TP24 to TP23, TP25 to TP24, TP26 to TP25, TP27 to TP26, TP28 to TP27, TP29 to TP28, TP30 to TP29, TP31 to TP30, TP32 to TP31, TP33 to TP32, TP34 to TP33, TP35 to TP34, TP36 to TP35, TP37 to TP36, TP38 to TP37, TP39 to TP38, TP40 to TP39, TP41 to TP40, TP42 to TP41, TP43 to TP42, TP44 to TP43, TP45 to TP44, TP46 to TP45, TP47 to TP46, TP48 to TP47, TP49 to TP48, TP50 to TP49, TP51 to TP50, TP52 to TP51, TP53 to TP52, TP54 to TP53, TP55 to TP54, TP56 to TP55, TP57 to TP56, TP58 to TP57, TP59 to TP58, TP60 to TP59, TP61 to TP60, TP62 to TP61, TP63 to TP62, TP64 to TP63, TP65 to TP64, TP66 to TP65, TP67 to TP66, TP68 to TP67, TST-R27 to TST-R21, TST-R21 to TST-R22, TST-R22 to TST-R23, TST-R23 to TST-R24, TST-R24 to TST-R25, TST-R25 to TST-R26, TST-R26 to TST-R27
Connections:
- BOOT1 pad 1: Earth -> /CHIP_BOOT
- BOOT1 pad 2: /CHIP_BOOT -> unconnected-(BOOT1-B-Pad2)
- BOOT2 pad 1: Earth -> /2CHIP_BOOT
- BOOT2 pad 2: /2CHIP_BOOT -> unconnected-(BOOT2-B-Pad2)
- PB1 pad 1: /7SEG.SEG1 -> unconnected-(PB1-A-Pad1)
- PB2 pad 1: /7SEG.SEG1 -> unconnected-(PB2-A-Pad1)
- R4 pad 1: /USB_CC2 -> /USB_CC1
- R5 pad 1: /USB_CC1 -> /USB_CC2
- R6 pad 1: /2USB_CC2 -> /2USB_CC1
- R7 pad 1: /2USB_CC1 -> /2USB_CC2
- RST2 pad 1: Earth -> /CHIP_PU
- RST2 pad 2: /2CHIP_PU -> unconnected-(RST2-B-Pad2)
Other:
- outline, holes or cut-outs redrawn

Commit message: draft commit
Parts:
- R8: value 450k -> 450kΩ
- Y1, Y2: value 40MHz -> 40MHz, 15pF; footprint Crystal:Crystal_SMD_3225-4Pin_3.2x2.5mm -> JLCPCB:OSC-SMD_4P-L3.2-W2.5-BL_SIT8008BI
- moved C4 0.22 mm to (71.5, 117.1)
- moved Y2 0.13 mm to (69.2, 117.1)
- moved Y1 0.07 mm to (79.9, 78.2)
- turned U4 to -90 degrees

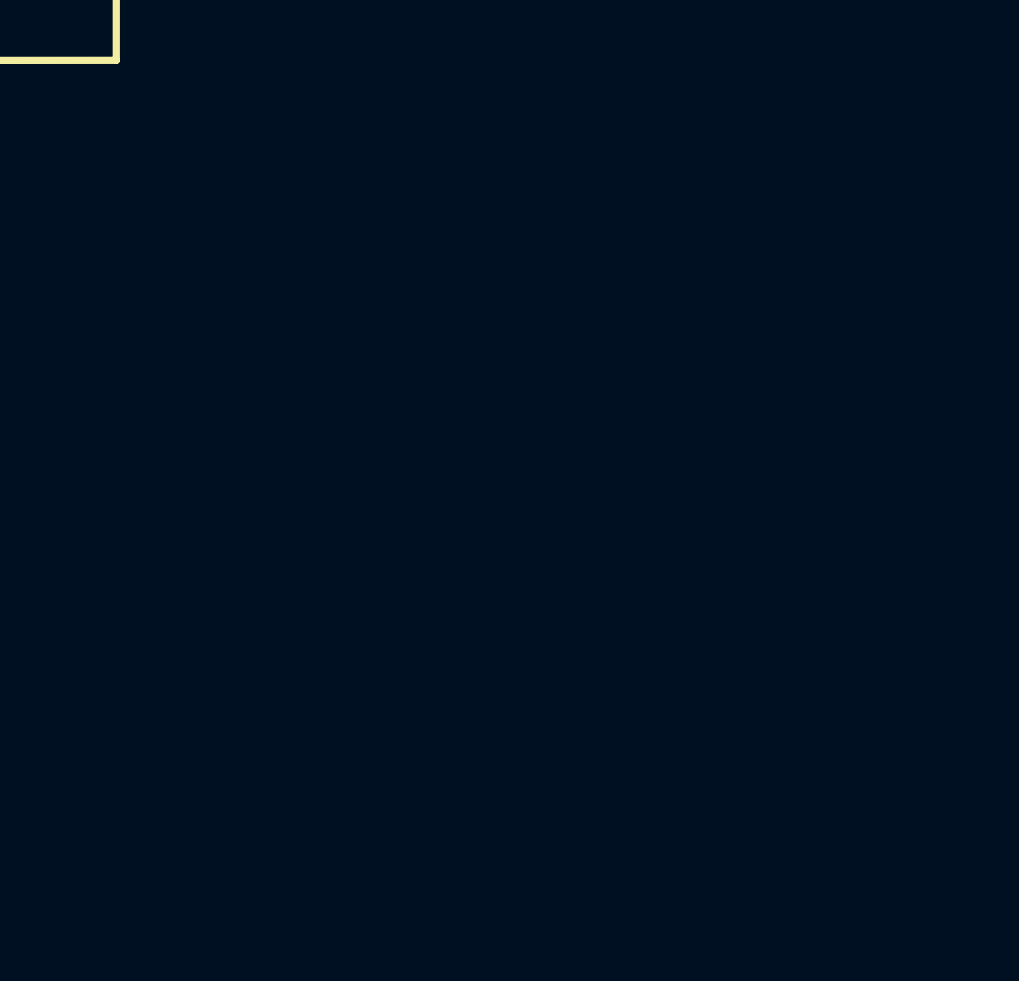
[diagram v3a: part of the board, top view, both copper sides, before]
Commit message: DRAFT added AXP2101 battery circuit
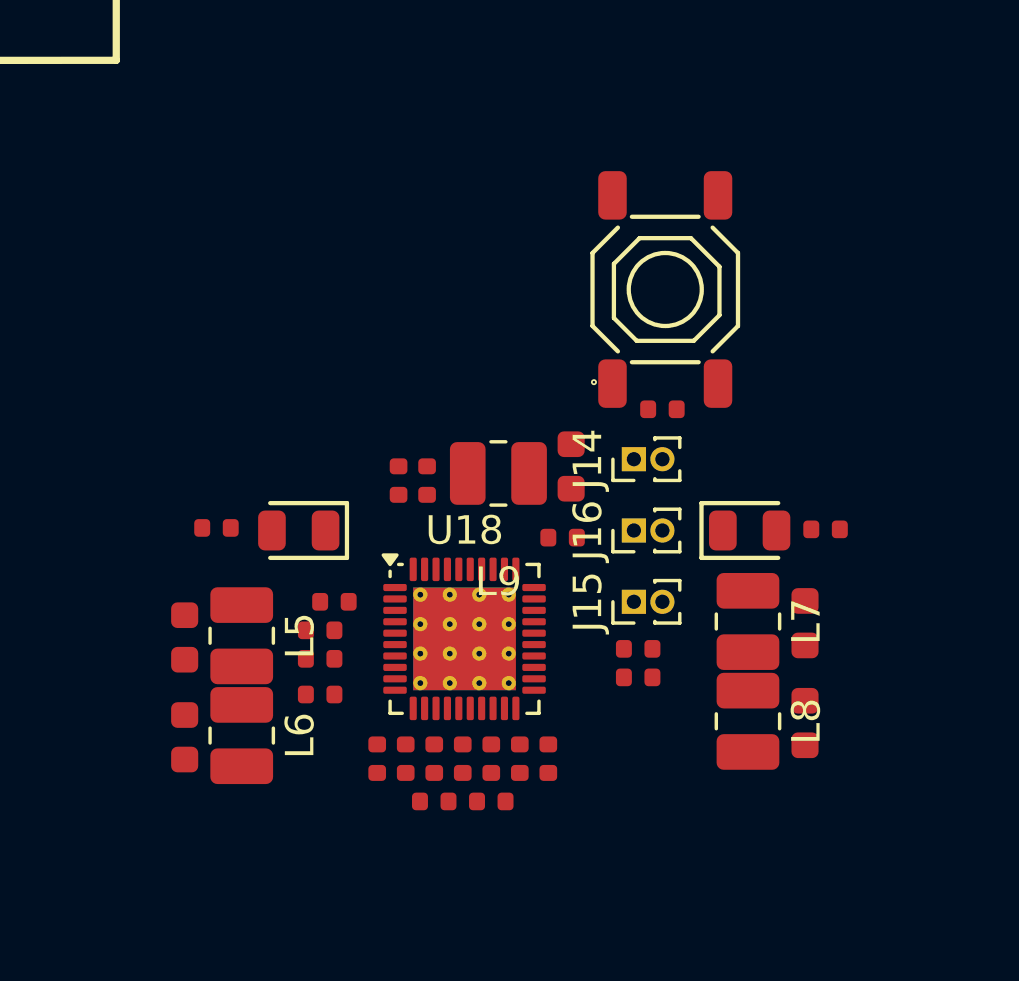
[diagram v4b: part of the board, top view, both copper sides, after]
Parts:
- added C73: 1uF, PCM_JLCPCB:C_0402, F.Cu at (127.2, 71.8)
- added C74: 10uF, PCM_JLCPCB:C_0402, F.Cu at (137.9, 74.4)
- added C75: 22uF, PCM_JLCPCB:C_0603, F.Cu at (122.0, 73.0)
- added C76: 22uF, PCM_JLCPCB:C_0603, F.Cu at (122.0, 76.5)
- added C77: 22uF, PCM_JLCPCB:C_0603, F.Cu at (143.8, 72.5)
- added C78: 22uF, PCM_JLCPCB:C_0603, F.Cu at (143.8, 76.0)
- added C79: 2.2uF, PCM_JLCPCB:C_0402, F.Cu at (132.8, 77.2)
- added C80: 2.2uF, PCM_JLCPCB:C_0402, F.Cu at (132.8, 78.8)
- added C81: 2.2uF, PCM_JLCPCB:C_0402, F.Cu at (131.8, 77.2)
- added C82: 2.2uF, PCM_JLCPCB:C_0402, F.Cu at (133.8, 77.2)
- added C83: 2.2uF, PCM_JLCPCB:C_0402, F.Cu at (134.8, 77.2)
- added C84: 2.2uF, PCM_JLCPCB:C_0402, F.Cu at (129.8, 77.2)
- added C85: 2.2uF, PCM_JLCPCB:C_0402, F.Cu at (130.8, 78.8)
- added C86: 2.2uF, PCM_JLCPCB:C_0402, F.Cu at (126.8, 75.0)
- added C87: 2.2uF, PCM_JLCPCB:C_0402, F.Cu at (128.8, 77.2)
- added C88: 1uF, PCM_JLCPCB:C_0402, F.Cu at (126.8, 73.8)
- added C89: 4.7uF, PCM_JLCPCB:C_0402, F.Cu at (129.5, 67.5)
- added C90: 1uF, PCM_JLCPCB:C_0402, F.Cu at (135.2, 69.5)
- added C91: 1uF, PCM_JLCPCB:C_0402, F.Cu at (130.5, 67.5)
- added C92: 1uF, PCM_JLCPCB:C_0402, F.Cu at (130.8, 77.2)
- added C93: 1uF, PCM_JLCPCB:C_0402, F.Cu at (126.8, 72.8)
- added C94: 1uF, PCM_JLCPCB:C_0402, F.Cu at (137.9, 73.4)
- added C95: 22uF, PCM_JLCPCB:C_0603, F.Cu at (135.6, 67.0)
- added C96: 2.2uF, PCM_JLCPCB:C_0402, F.Cu at (138.8, 65.0)
- added D14: Yellow, PCM_JLCPCB:D_0805, F.Cu at (126.0, 69.2)
- added D15: Green, PCM_JLCPCB:D_0805, F.Cu at (141.8, 69.2)
- added J14: Conn_01x02, Connector_PinHeader_1.00mm:PinHeader_1x02_P1.00mm_Vertical, F.Cu at (137.8, 66.8)
- added J15: Conn_01x02, Connector_PinHeader_1.00mm:PinHeader_1x02_P1.00mm_Vertical, F.Cu at (137.8, 71.8)
- added J16: Conn_01x02, Connector_PinHeader_1.00mm:PinHeader_1x02_P1.00mm_Vertical, F.Cu at (137.8, 69.2)
- added L5: 1uH,3.3A, Inductor_SMD:L_1008_2520Metric, F.Cu at (124.0, 72.9)
- added L6: 1uH,3.3A, Inductor_SMD:L_1008_2520Metric, F.Cu at (124.0, 76.4)
- added L7: 1uH,3.3A, Inductor_SMD:L_1008_2520Metric, F.Cu at (141.8, 72.4)
- added L8: 1uH,3.3A, Inductor_SMD:L_1008_2520Metric, F.Cu at (141.8, 75.9)
- added L9: 1uH,3.3A, Inductor_SMD:L_1008_2520Metric, F.Cu at (133.0, 67.2)
- added PB3: Tactile Button, 160gf, PCM_JLCPCB:SW-SMD_4P-L5.1-W5.1-P3.70-LS6.5-TL-2, F.Cu at (138.8, 60.8)
- added R66: 10kΩ, PCM_JLCPCB:R_0402, F.Cu at (123.1, 69.2)
- added R67: 10kΩ, PCM_JLCPCB:R_0402, F.Cu at (144.5, 69.2)
- added U18: AXP2101, Package_DFN_QFN:QFN-40-1EP_5x5mm_P0.4mm_EP3.6x3.6mm_ThermalVias, F.Cu at (131.8, 73.0)
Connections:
- net /2GPIO37 renamed /BAT.SCK
- net /2GPIO38 renamed /BAT.SDA

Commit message: DRAFT added misc outputs, PMU and resolved some TODO notes.
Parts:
- added BT1: BH-18650-B1BA002, JLCPCB:BATTERY-SMD_18650-1S-L77.1-W20.7-1, F.Cu at (169.8, 98.9)
- added C97: 22uF, PCM_JLCPCB:C_0603, F.Cu at (134.5, 64.8)
- added D16: IR, JLCPCB:IR-LED_C131280, F.Cu at (95.5, 129.0)
- added D17: IR, JLCPCB:IR-LED_C131280, F.Cu at (95.5, 122.8)
- added D18: IR, JLCPCB:IR-LED_C131280, F.Cu at (95.5, 116.6)
- added J17: Conn_01x02, Connector_PinHeader_1.00mm:PinHeader_1x02_P1.00mm_Vertical, F.Cu at (93.0, 130.5)
- added J18: Conn_01x02, Connector_PinHeader_1.00mm:PinHeader_1x02_P1.00mm_Vertical, F.Cu at (93.0, 124.2)
- added J19: Conn_01x02, Connector_PinHeader_1.00mm:PinHeader_1x02_P1.00mm_Vertical, F.Cu at (93.0, 118.1)
- added NTC1: NTC, PCM_JLCPCB:R_0402, F.Cu at (140.5, 67.0)
- added PB4: Tactile Button, 160gf, PCM_JLCPCB:SW-SMD_4P-L5.1-W5.1-P3.70-LS6.5-TL-2, F.Cu at (129.0, 48.2)
- added PB5: Tactile Button, 160gf, PCM_JLCPCB:SW-SMD_4P-L5.1-W5.1-P3.70-LS6.5-TL-2, F.Cu at (73.0, 48.2)
- added Q6: AO3401A, PCM_JLCPCB:Q_SOT-23, F.Cu at (92.3, 127.5)
- added Q7: AO3401A, PCM_JLCPCB:Q_SOT-23, F.Cu at (92.3, 121.2)
- added Q8: AO3401A, PCM_JLCPCB:Q_SOT-23, F.Cu at (92.3, 115.0)
- added R68: 100kΩ, PCM_JLCPCB:R_0402, F.Cu at (72.8, 134.0)
- added R69: 10kΩ, PCM_JLCPCB:R_0402, F.Cu at (70.8, 134.0)
- added R70: 10kΩ, PCM_JLCPCB:R_0402, F.Cu at (81.0, 128.2)
- added R71: 100kΩ, PCM_JLCPCB:R_0402, F.Cu at (81.0, 126.2)
- added R72: 100kΩ, PCM_JLCPCB:R_0402, F.Cu at (64.8, 126.8)
- added R73: 10kΩ, PCM_JLCPCB:R_0402, F.Cu at (64.8, 128.7)
- added R74: 220kΩ, PCM_JLCPCB:R_0402, F.Cu at (132.8, 110.5)
- added R75: 10kΩ, PCM_JLCPCB:R_0402, F.Cu at (132.8, 111.5)
- added R76: 220kΩ, PCM_JLCPCB:R_0402, F.Cu at (132.8, 109.5)
- added R77: 1MΩ, PCM_JLCPCB:R_0402, F.Cu at (89.8, 126.5)
- added R78: 10kΩ, PCM_JLCPCB:R_0402, F.Cu at (95.2, 126.2)
- added R79: 10MΩ, PCM_JLCPCB:R_0402, F.Cu at (89.8, 122.2)
- added R8: 10MΩ, PCM_JLCPCB:R_0402, F.Cu at (89.8, 128.5)
- added R80: 1MΩ, PCM_JLCPCB:R_0402, F.Cu at (89.8, 120.2)
- added R81: 10kΩ, PCM_JLCPCB:R_0402, F.Cu at (95.2, 120.0)
- added R82: 10MΩ, PCM_JLCPCB:R_0402, F.Cu at (89.8, 116.0)
- added R83: 1MΩ, PCM_JLCPCB:R_0402, F.Cu at (89.8, 114.0)
- added R84: 10kΩ, PCM_JLCPCB:R_0402, F.Cu at (95.2, 113.8)
- added TP68: TestPoint, TestPoint:TestPoint_Pad_D1.0mm, F.Cu at (131.0, 63.8)
- added TP69: TestPoint, TestPoint:TestPoint_Loop_D3.50mm_Drill0.9mm_Beaded, F.Cu at (187.9, 29.7)
- added TP70: TestPoint, TestPoint:TestPoint_Loop_D3.50mm_Drill0.9mm_Beaded, F.Cu at (187.9, 35.0)
- added TP71: TestPoint, TestPoint:TestPoint_Loop_D3.50mm_Drill0.9mm_Beaded, F.Cu at (187.9, 40.2)
- added TP72: TestPoint, TestPoint:TestPoint_Loop_D3.50mm_Drill0.9mm_Beaded, F.Cu at (187.9, 45.5)
- added TP73: TestPoint, TestPoint:TestPoint_Loop_D3.50mm_Drill0.9mm_Beaded, F.Cu at (193.1, 29.7)
- added TP74: TestPoint, TestPoint:TestPoint_Loop_D3.50mm_Drill0.9mm_Beaded, F.Cu at (193.1, 35.0)
- added TP75: TestPoint, TestPoint:TestPoint_Loop_D3.50mm_Drill0.9mm_Beaded, F.Cu at (193.1, 40.2)
- added TP76: TestPoint, TestPoint:TestPoint_Loop_D3.50mm_Drill0.9mm_Beaded, F.Cu at (193.1, 45.5)
- added TP77: TestPoint, TestPoint:TestPoint_Loop_D3.50mm_Drill0.9mm_Beaded, F.Cu at (198.4, 29.7)
- added TP78: TestPoint, TestPoint:TestPoint_Loop_D3.50mm_Drill0.9mm_Beaded, F.Cu at (198.4, 35.0)
- added TP79: TestPoint, TestPoint:TestPoint_Loop_D3.50mm_Drill0.9mm_Beaded, F.Cu at (198.4, 40.2)
- added TP80: TestPoint, TestPoint:TestPoint_Loop_D3.50mm_Drill0.9mm_Beaded, F.Cu at (198.4, 45.5)
- added TP81: TestPoint, TestPoint:TestPoint_Loop_D3.50mm_Drill0.9mm_Beaded, F.Cu at (203.6, 29.7)
- added TP82: TestPoint, TestPoint:TestPoint_Loop_D3.50mm_Drill0.9mm_Beaded, F.Cu at (203.6, 35.0)
- added TP83: TestPoint, TestPoint:TestPoint_Loop_D3.50mm_Drill0.9mm_Beaded, F.Cu at (203.6, 40.2)
- added TP84: TestPoint, TestPoint:TestPoint_Loop_D3.50mm_Drill0.9mm_Beaded, F.Cu at (203.6, 45.5)
- added TST-R28: 0Ω, PCM_JLCPCB:R_0603, F.Cu at (139.0, 78.2)
- added TST-R29: 0Ω, PCM_JLCPCB:R_0603, F.Cu at (137.8, 78.2)
- added TST-R30: 0Ω, PCM_JLCPCB:R_0603, F.Cu at (89.5, 130.2)
- added TST-R31: 0Ω, PCM_JLCPCB:R_0603, F.Cu at (89.5, 124.0)
- added TST-R32: 0Ω, PCM_JLCPCB:R_0603, F.Cu at (89.5, 117.8)
- moved TP17 6.89 mm to (85.0, 135.2)
- moved TP18 6.89 mm to (85.0, 132.0)
- moved TP19 6.89 mm to (85.0, 129.0)
- moved TP20 6.89 mm to (85.0, 125.8)
- moved TP21 6.89 mm to (85.0, 122.8)
- moved TP22 6.89 mm to (85.0, 120.0)
- moved TP23 6.89 mm to (85.0, 117.2)
- moved TP24 6.89 mm to (85.0, 114.2)
- moved R33 6.43 mm to (92.5, 134.0), turned to 180 degrees
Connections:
- net /2GPIO14 renamed /VBus.Sense
- net /2GPIO2 renamed /3v3.Sense
- net /2GPIO33 renamed /PMU.Vo1.Sense
- net /2GPIO34 renamed /MISC.OUT1
- net /2GPIO35 renamed /MISC.OUT2
- net /2GPIO36 renamed /MISC.OUT3
- net /BAT.SCK renamed /PMU.SCK
- net /BAT.SDA renamed /PMU.SDA
- net Net-(U18-ALDO1) renamed /PMU.Va1
- net Net-(U18-ALDO2) renamed /PMU.Va2
- net Net-(U18-ALDO3) renamed /PMU.Va3
- net Net-(U18-ALDO4) renamed /PMU.Va4
- net Net-(U18-BLDO1) renamed /PMU.Vb1
- net Net-(U18-BLDO2) renamed /PMU.Vb2
- net Net-(U18-CPULDOS) renamed /PMU.Vcpu
- net Net-(U18-DLDO1/DC1SW) renamed /PMU.Vd1
- net Net-(U18-DLDO2/DC4SW) renamed /PMU.Vd2
- net Net-(U18-FB2) renamed /PMU.Vo2
- net Net-(U18-FB3) renamed /PMU.Vo3
- net Net-(U18-LX1) renamed /PMU.Vo1
- net Net-(U18-LX4) renamed /PMU.Vo4
- C73 pad 2: Net-(U18-VREF) -> /PMU.Vref
- C74 pad 1: VBUS -> Net-(U18-VBUS)
- C88 pad 2: VBUS -> /PMU.Vsys
- C89 pad 2: VBUS -> /PMU.Vsys
- C91 pad 2: VBUS -> /PMU.Vsys
- C92 pad 2: VBUS -> /PMU.Vsys
- C93 pad 2: VBUS -> /PMU.Vsys
- C94 pad 2: VBUS -> /PMU.Vsys
- R66 pad 2: VBUS -> /PMU.Vsys
- R67 pad 2: VBUS -> /PMU.Vsys
- TP16 pad 1: /2GPIO26 -> /PMU.Vref
- U18 pad 13: VBUS -> /PMU.Vsys
- U18 pad 17: VBUS -> /PMU.Vsys
- U18 pad 2: Net-(U18-VREF) -> /PMU.Vref
- U18 pad 23: VBUS -> /PMU.Vsys
- U18 pad 24: VBUS -> /PMU.Vsys
- U18 pad 34: VBUS -> /PMU.Vsys
- U18 pad 36: VBUS -> /PMU.Vsys
- U18 pad 37: VBUS -> Net-(U18-VBUS)
- U18 pad 38: unconnected-(U18-IRQ-Pad38) -> Net-(U18-IRQ)
- U18 pad 6: VBUS -> /PMU.Vsys
- U18 pad 7: VBUS -> /PMU.Vsys
- U8 pad 28: /2GPIO26 -> /PMU.Vref
